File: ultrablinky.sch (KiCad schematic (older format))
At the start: 124 parts, among them J1 DNP, J2 SJ1-3523N, J3 SJ1-3523N, J4 Barrel_Jack_5.5x2.5, J5 DNP, J6 DNP, J7 Terminal5, J8 SJ1-3523N, Q1 DMP6180SK3Q-13, Q2 DMP6180SK3Q-13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

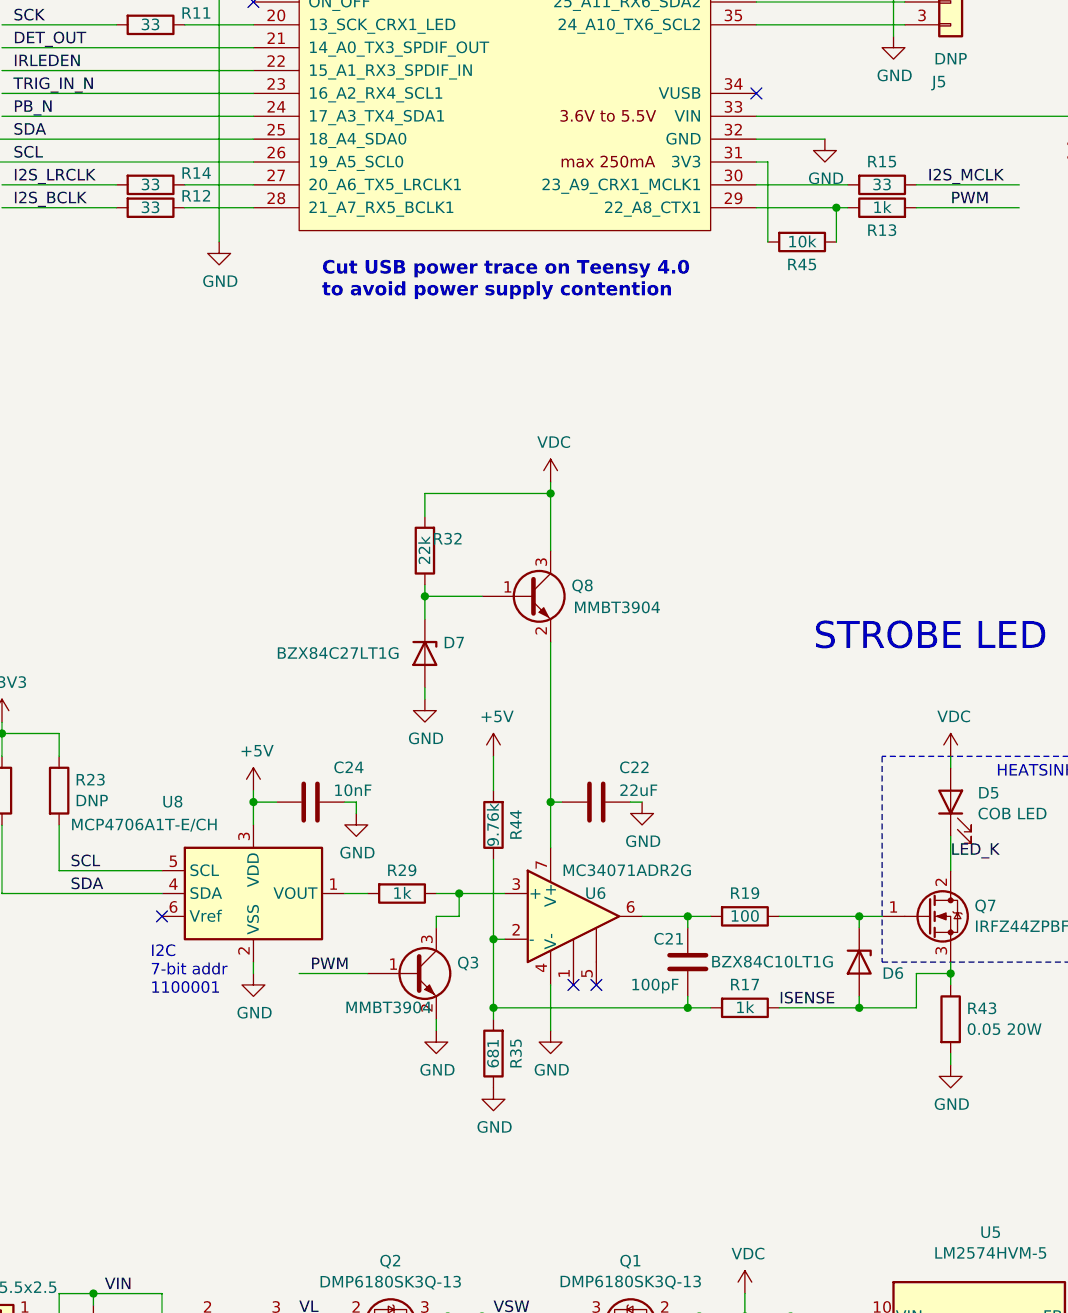
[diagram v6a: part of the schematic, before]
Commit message: Fixed inverted logic of PWM enable
The NPN transistor has now been replaced with a 74VHC1G09 open-drain
driver. This means that when the PWM output of the Teensy is low, the
DAC will also be low instead of being inverted
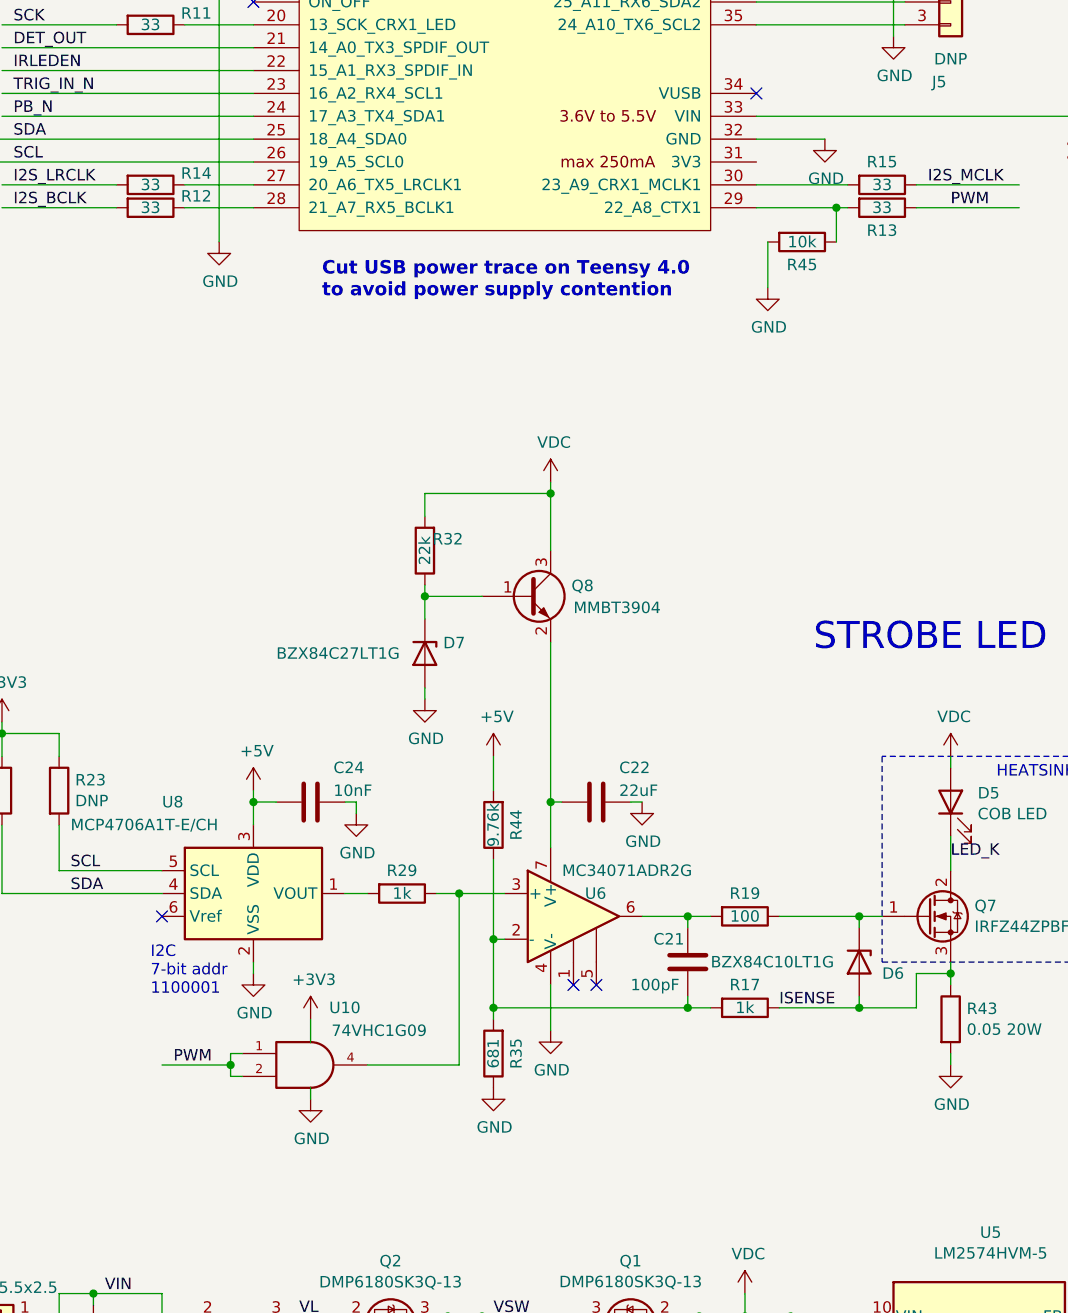
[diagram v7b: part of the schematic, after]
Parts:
- removed Q3: MMBT3904, Package_TO_SOT_SMD:SOT-23, symbol Transistor_BJT:MMBT3904
- added U10: 74VHC1G09, Package_TO_SOT_SMD:SOT-353_SC-70-5, symbol 74xGxx:74AHC1G08
- R13: value 1k -> 33; Source Mouser 603-RC0805JR-071KL -> Mouser 603-RC0805JR-1333RL
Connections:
- wire segments 380 -> 383
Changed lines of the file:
@@
 Wire Wire Line
 	3200 6650 3300 6650
-$Comp
-L power:GND #PWR0115
-U 1 1 602D3CB0
-P 3200 7250
-F 0 "#PWR0115" H 3200 7000 50  0001 C CNN
-F 1 "GND" H 3205 7077 50  0000 C CNN
-F 2 "" H 3200 7250 50  0001 C CNN
-F 3 "" H 3200 7250 50  0001 C CNN
-	1    3200 7250
-	1    0    0    -1
-$EndComp
-Wire Wire Line
-	3200 7250 3200 7200
-Wire Wire Line
-	3200 6800 3200 6750
-Wire Wire Line
-	3200 6750 3300 6750
-Wire Wire Line
-	3300 6750 3300 6650
 Connection ~ 3300 6650
 Wire Wire Line
@@
 Wire Wire Line
 	3700 7050 3700 7250
-Text Label 2650 7000 0    50   ~ 0
+Text Label 2050 7400 0    50   ~ 0
 PWM
 Text Label 5450 3650 0    50   ~ 0
@@
 	1    0    0    -1
 $EndComp
-$Comp
-L Device:R R13
-U 1 1 603080FE
-P 5150 3650
-F 0 "R13" V 5050 3650 50  0000 C CNN
-F 1 "1k" V 5150 3650 50  0000 C CNN
-F 2 "Resistor_SMD:R_0805_2012Metric" V 5080 3650 50  0001 C CNN
-F 3 "~" H 5150 3650 50  0001 C CNN
-F 4 "Mouser 603-RC0805JR-071KL" H 5150 3650 50  0001 C CNN "Source"
-	1    5150 3650
-	0    -1   -1   0
-$EndComp
 Wire Wire Line
 	2150 8500 2000 8500
@@
 IRLEDEN
 Wire Wire Line
-	2600 7000 2900 7000
-Wire Wire Line
 	5450 6950 5450 7000
 Wire Wire Line
@@
 I2C\n7-bit addr\n0001010
 $Comp
-L Transistor_BJT:MMBT3904 Q3
-U 1 1 60D6FD7B
-P 3100 7000
-F 0 "Q3" H 3291 7046 50  0000 L CNN
-F 1 "MMBT3904" H 2800 6850 50  0000 L CNN
-F 2 "Package_TO_SOT_SMD:SOT-23" H 3300 6925 50  0001 L CIN
-F 3 "http://www.onsemi.com/pdf/datasheet/mmbt3904lt1-d.pdf" H 3100 7000 50  0001 L CNN
-F 4 "Mouser 863-MMBT3904LT3G" H 3100 7000 50  0001 C CNN "Source"
-	1    3100 7000
-	1    0    0    -1
-$EndComp
-$Comp
 L 0_my_symbols:AudioJack3_CUI_SJ1-3523N J?
 U 1 1 60DE06CA
@@
 	4600 3350 4900 3350
 Wire Wire Line
-	4600 3450 4650 3450
-Wire Wire Line
-	4650 3450 4650 3800
+	4650 4000 4650 3800
 Wire Wire Line
 	4950 3800 4950 3650
@@
 $EndComp
 NoConn ~ 2000 6750
+$Comp
+L power:GND #PWR08
+U 1 1 60CB8449
+P 2650 7550
+F 0 "#PWR08" H 2650 7300 50  0001 C CNN
+F 1 "GND" H 2655 7377 50  0000 C CNN
+F 2 "" H 2650 7550 50  0001 C CNN
+F 3 "" H 2650 7550 50  0001 C CNN
+	1    2650 7550
+	1    0    0    -1
+$EndComp
+Wire Wire Line
+	2650 7550 2650 7500
+$Comp
+L 74xGxx:74AHC1G08 U10
+U 1 1 60CE47C1
+P 2650 7400
+F 0 "U10" H 2800 7650 50  0000 C CNN
+F 1 "74VHC1G09" H 2950 7550 50  0000 C CNN
+F 2 "Package_TO_SOT_SMD:SOT-353_SC-70-5" H 2650 7400 50  0001 C CNN
+F 3 "" H 2650 7400 50  0001 C CNN
+	1    2650 7400
+	1    0    0    -1
+$EndComp
+$Comp
+L power:+3V3 #PWR07
+U 1 1 60D178AB
+P 2650 7200
+F 0 "#PWR07" H 2650 7050 50  0001 C CNN
+F 1 "+3V3" H 2665 7373 50  0000 C CNN
+F 2 "" H 2650 7200 50  0001 C CNN
+F 3 "" H 2650 7200 50  0001 C CNN
+	1    2650 7200
+	1    0    0    -1
+$EndComp
+Wire Wire Line
+	2650 7200 2650 7300
+Wire Wire Line
+	2350 7350 2300 7350
+Wire Wire Line
+	2300 7350 2300 7400
+Wire Wire Line
+	2300 7450 2350 7450
+Wire Wire Line
+	2900 7400 3300 7400
+Wire Wire Line
+	3300 6650 3300 7400
+Wire Wire Line
+	2300 7400 2000 7400
+Connection ~ 2300 7400
+Wire Wire Line
+	2300 7400 2300 7450
+$Comp
+L power:GND #PWR09
+U 1 1 60EB12C1
+P 4650 4000
+F 0 "#PWR09" H 4650 3750 50  0001 C CNN
+F 1 "GND" H 4655 3827 50  0000 C CNN
+F 2 "" H 4650 4000 50  0001 C CNN
+F 3 "" H 4650 4000 50  0001 C CNN
+	1    4650 4000
+	1    0    0    -1
+$EndComp
+$Comp
+L Device:R R13
+U 1 1 60EB168F
+P 5150 3650
+F 0 "R13" V 5250 3650 50  0000 C CNN
+F 1 "33" V 5150 3650 50  0000 C CNN
+F 2 "Resistor_SMD:R_0805_2012Metric" V 5080 3650 50  0001 C CNN
+F 3 "~" H 5150 3650 50  0001 C CNN
+F 4 "Mouser 603-RC0805JR-1333RL" H 5150 3650 50  0001 C CNN "Source"
+	1    5150 3650
+	0    1    1    0
+$EndComp
 $EndSCHEMATC

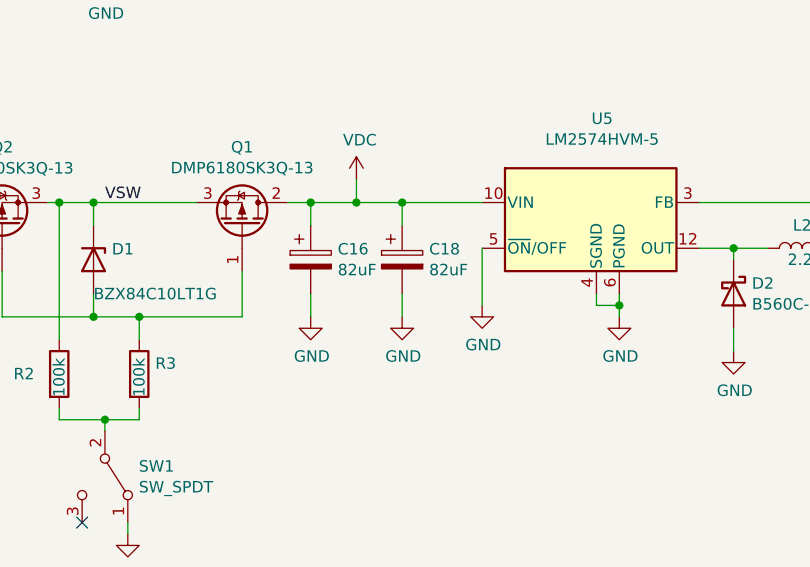
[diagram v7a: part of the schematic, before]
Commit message: Increased bus cap to 3300uF
The bus capacitance needs to be high enough to allow for short pulses of
much higher current than the power supply can put out so a large value
is needed
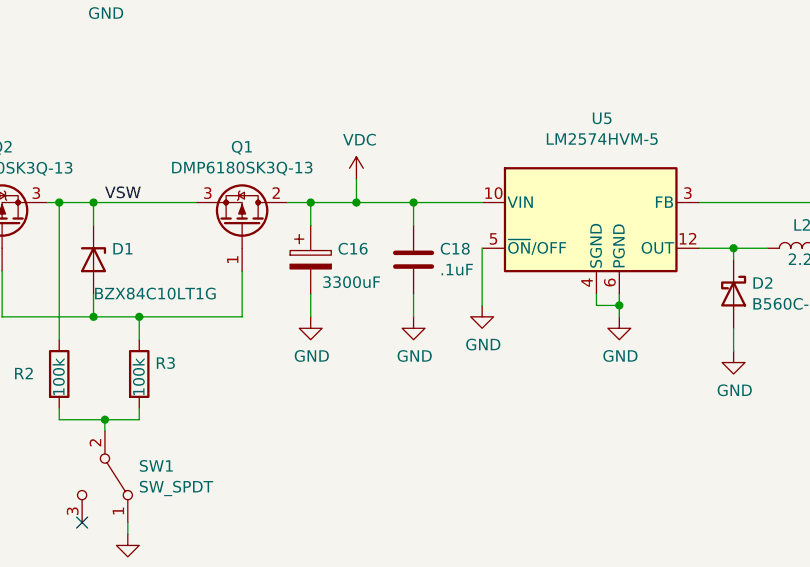
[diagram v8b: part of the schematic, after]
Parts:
- removed C18: 82uF, Capacitor_SMD:CP_Elec_10x10, symbol Device:CP
- added C18: .1uF, Resistor_SMD:R_0805_2012Metric, symbol Device:C
- C16: value 82uF -> 3300uF; footprint Capacitor_SMD:CP_Elec_10x10 -> 0_my_footprints:CP_Radial_L40.0mm_D20.0mm_P7.50mm_Horizontal; Source Mouser 667-EEE-FN1K820UL -> Mouser 647-UFW1J332MRD, LCSC Ymin LKMJ4001J333MF
- U10: Source (none) -> Mouser 863-MC74VHC1G09DFT2G
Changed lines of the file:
@@
 P 4350 8750
 F 0 "C16" H 4468 8796 50  0000 L CNN
-F 1 "82uF" H 4468 8705 50  0000 L CNN
-F 2 "Capacitor_SMD:CP_Elec_10x10" H 4388 8600 50  0001 C CNN
+F 1 "3300uF" H 4400 8650 50  0000 L CNN
+F 2 "0_my_footprints:CP_Radial_L40.0mm_D20.0mm_P7.50mm_Horizontal" H 4388 8600 50  0001 C CNN
 F 3 "~" H 4350 8750 50  0001 C CNN
-F 4 "Mouser 667-EEE-FN1K820UL" H 4350 8750 50  0001 C CNN "Source"
+F 4 "Mouser 647-UFW1J332MRD, LCSC Ymin LKMJ4001J333MF" H 4350 8750 50  0001 C CNN "Source"
 	1    4350 8750
 	1    0    0    -1
@@
 	1    0    0    -1
 $EndComp
-Wire Wire Line
-	4550 8500 4750 8500
 $Comp
 L power:+5V #PWR0121
@@
 	1    0    0    -1
 $EndComp
-$Comp
-L Device:CP C18
-U 1 1 6066DBF2
-P 4750 8750
-F 0 "C18" H 4868 8796 50  0000 L CNN
-F 1 "82uF" H 4868 8705 50  0000 L CNN
-F 2 "Capacitor_SMD:CP_Elec_10x10" H 4788 8600 50  0001 C CNN
-F 3 "~" H 4750 8750 50  0001 C CNN
-F 4 "Mouser 667-EEE-FN1K820UL" H 4750 8750 50  0001 C CNN "Source"
-	1    4750 8750
-	1    0    0    -1
-$EndComp
 Wire Wire Line
-	4750 8600 4750 8500
+	4800 8600 4800 8500
 $Comp
 L power:GND #PWR0185
 U 1 1 60691F6B
-P 4750 9000
-F 0 "#PWR0185" H 4750 8750 50  0001 C CNN
-F 1 "GND" H 4755 8827 50  0000 C CNN
-F 2 "" H 4750 9000 50  0001 C CNN
-F 3 "" H 4750 9000 50  0001 C CNN
-	1    4750 9000
+P 4800 9000
+F 0 "#PWR0185" H 4800 8750 50  0001 C CNN
+F 1 "GND" H 4805 8827 50  0000 C CNN
+F 2 "" H 4800 9000 50  0001 C CNN
+F 3 "" H 4800 9000 50  0001 C CNN
+	1    4800 9000
 	1    0    0    -1
 $EndComp
 Wire Wire Line
-	4750 8900 4750 9000
+	4800 8900 4800 9000
 Text Label 5450 6500 0    50   ~ 0
 LED_K
@@
 VL
 Connection ~ 4350 8500
-Connection ~ 4750 8500
 Wire Wire Line
 	4350 8500 4550 8500
-Wire Wire Line
-	4750 8500 5100 8500
 Text Label 3450 8500 0    50   ~ 0
 VSW
@@
 F 1 "74VHC1G09" H 2950 7550 50  0000 C CNN
 F 2 "Package_TO_SOT_SMD:SOT-353_SC-70-5" H 2650 7400 50  0001 C CNN
-F 3 "" H 2650 7400 50  0001 C CNN
+F 3 "https://www.onsemi.com/pdf/datasheet/mc74vhc1g09-d.pdf" H 2650 7400 50  0001 C CNN
+F 4 "Mouser 863-MC74VHC1G09DFT2G" H 2650 7400 50  0001 C CNN "Source"
 	1    2650 7400
 	1    0    0    -1
@@
 	0    1    1    0
 $EndComp
+$Comp
+L Device:C C?
+U 1 1 60F00028
+P 4800 8750
+AR Path="/5ECF51E5/60F00028" Ref="C?"  Part="1"
+AR Path="/60F00028" Ref="C18"  Part="1"
+AR Path="/60675ACD/60F00028" Ref="C?"  Part="1"
+F 0 "C18" H 4915 8796 50  0000 L CNN
+F 1 ".1uF" H 4915 8705 50  0000 L CNN
+F 2 "Resistor_SMD:R_0805_2012Metric" H 4838 8600 50  0001 C CNN
+F 3 "~" H 4800 8750 50  0001 C CNN
+F 4 "Mouser 80-C0805C104K5R" H 4800 8750 50  0001 C CNN "Source"
+	1    4800 8750
+	1    0    0    -1
+$EndComp
+Connection ~ 4800 8500
+Wire Wire Line
+	4800 8500 5100 8500
+Wire Wire Line
+	4550 8500 4800 8500
 $EndSCHEMATC
